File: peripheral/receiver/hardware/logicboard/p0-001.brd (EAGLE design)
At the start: 23 x 72 mm, 14 parts, among them IC1 74LS07N, IC2 LTC485N

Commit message: Clean up of document, schematic, and board design.
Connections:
- net GND: no longer JP1.3, MIDIOUT.3
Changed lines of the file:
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@@
 <contactref element="JP1" pad="2"/>
 <contactref element="JP2" pad="2"/>
-<contactref element="MIDIOUT" pad="3"/>
-<contactref element="JP1" pad="3"/>
 <wire x1="10.5" y1="56" x2="16" y2="53.46" width="0" layer="19" extent="1-1"/>
-<wire x1="16" y1="36.5" x2="16" y2="53.46" width="0" layer="19" extent="1-1"/>
-<wire x1="16" y1="33.96" x2="16" y2="36.5" width="0" layer="19" extent="1-1"/>
-<wire x1="10.5" y1="36.5" x2="16" y2="36.5" width="0" layer="19" extent="1-1"/>
-<wire x1="10.5" y1="29.2" x2="16" y2="33.96" width="0" layer="19" extent="1-1"/>
-<wire x1="9.81" y1="25.81" x2="10.5" y2="29.2" width="0" layer="19" extent="1-1"/>
+<wire x1="10.5" y1="36.5" x2="16" y2="53.46" width="0" layer="19" extent="1-1"/>
+<wire x1="16" y1="33.96" x2="10.5" y2="36.5" width="0" layer="19" extent="1-1"/>
+<wire x1="9.81" y1="25.81" x2="16" y2="33.96" width="0" layer="19" extent="1-1"/>
 <wire x1="15" y1="20.73" x2="9.81" y2="25.81" width="0" layer="19" extent="1-1"/>
 <wire x1="9.81" y1="18.19" x2="15" y2="20.73" width="0" layer="19" extent="1-1"/>

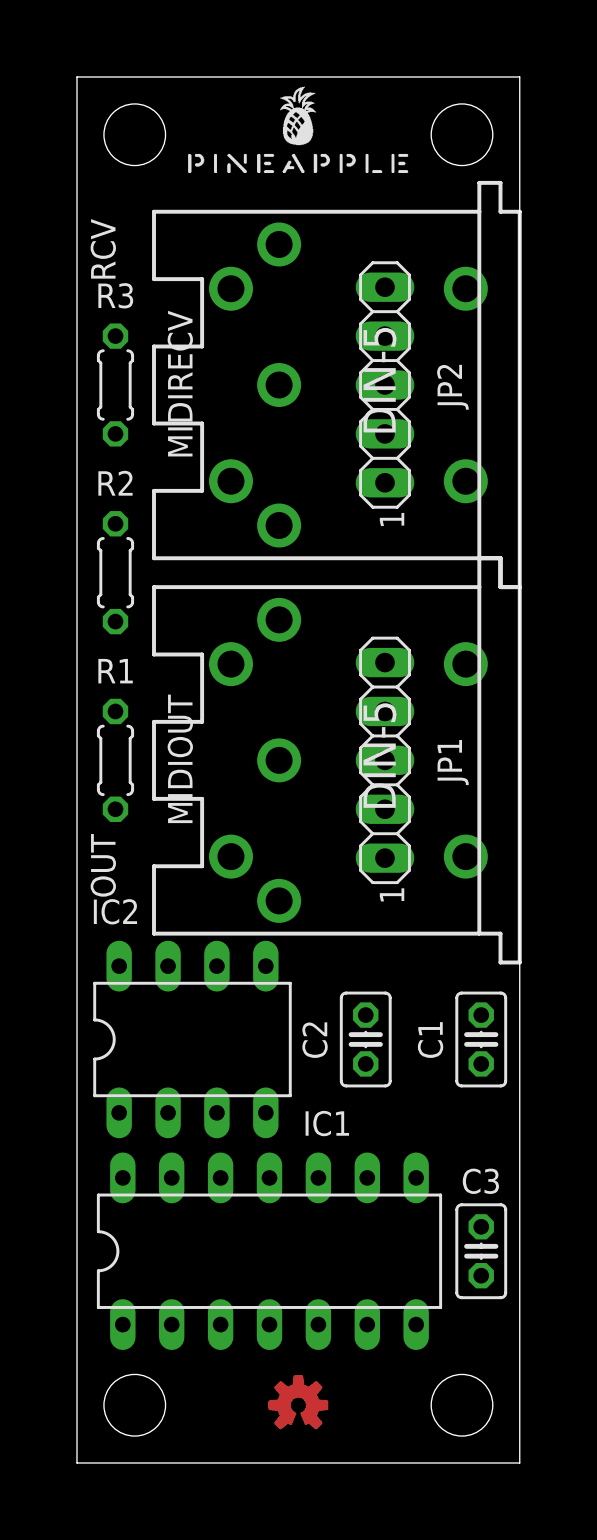
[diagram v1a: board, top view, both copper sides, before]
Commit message: Changed connectors of longrange receiver.
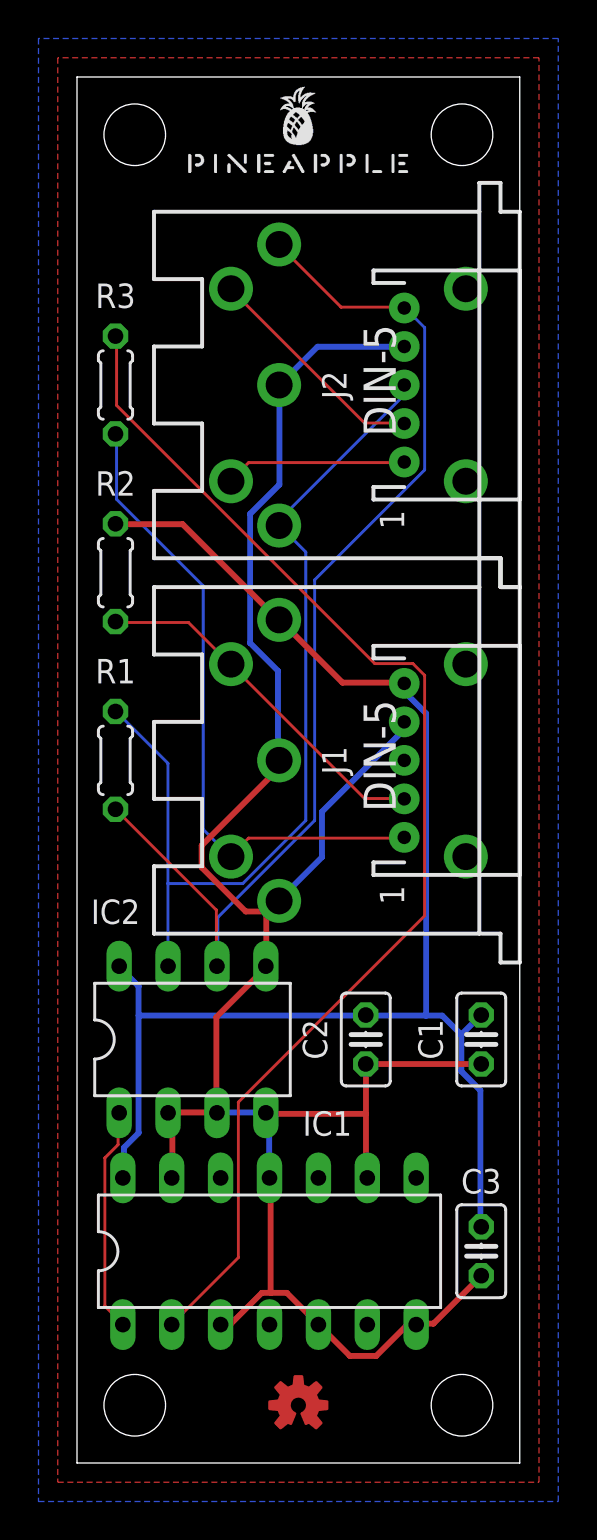
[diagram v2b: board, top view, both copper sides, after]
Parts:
- removed JP1, JP2: (no value), pinhead:1X05
- added J1, J2: (no value), SparkFun-Connectors:JST-5-PTH
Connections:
- net DUMMY4: now also J2.4; no longer JP2.4
- net DUMMY5: now also J2.5; no longer JP2.5
- net GND: now also J1.2, J2.2, MIDIOUT.3; no longer JP1.2, JP2.2
- net MIDIOUTRTN: now also J1.5; no longer JP1.5
- net MIDIOUTSND: now also J1.4; no longer JP1.4
- net RX+: now also J2.1; no longer JP2.1
- net RX-: now also J2.3; no longer JP2.3
- net VCC: now also J1.1; no longer JP1.1
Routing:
- net GND: track 0.00 -> 117.5 mm
- net VCC: track 0.00 -> 77.0 mm
- net N$1: track 0.00 -> 64.6 mm
- net RX+: track 0.00 -> 57.4 mm
- net RX-: track 0.00 -> 48.8 mm
- net MIDIOUTRTN: track 0.00 -> 33.9 mm
- net MIDIOUTSND: track 0.00 -> 18.8 mm
- net DUMMY4: track 0.00 -> 11.9 mm
- net TX: track 0.00 -> 11.7 mm
- net DUMMY5: track 0.00 -> 9.46 mm
- added copper zone on layer 1, net GND
- added copper zone on layer 16, net GND
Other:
- board text added: "GND"
- board text added: "NC"
- board text added: "RX+"
- board text added: "RX-"
- board text added: "Return"
- board text added: "Send"
- board text added: "Vcc"
- board text removed: "OUT"
- board text removed: "RCV"
